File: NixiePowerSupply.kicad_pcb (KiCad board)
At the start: 2 copper layers, 50.8 x 38.1 mm, 12 parts, among them J1 BARREL_JACK, T1 IRF644, U1 MAX1771

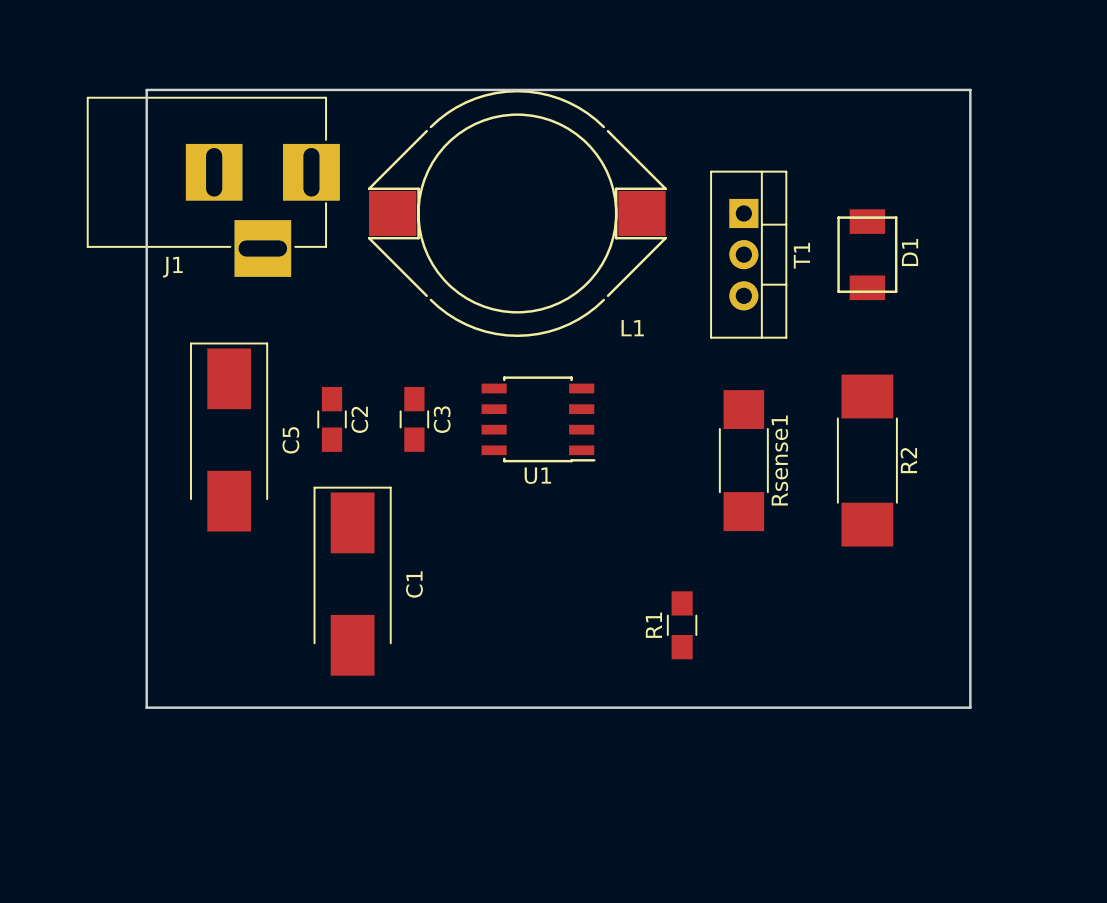
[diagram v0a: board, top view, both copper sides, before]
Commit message: Added cap and trimpot footprints
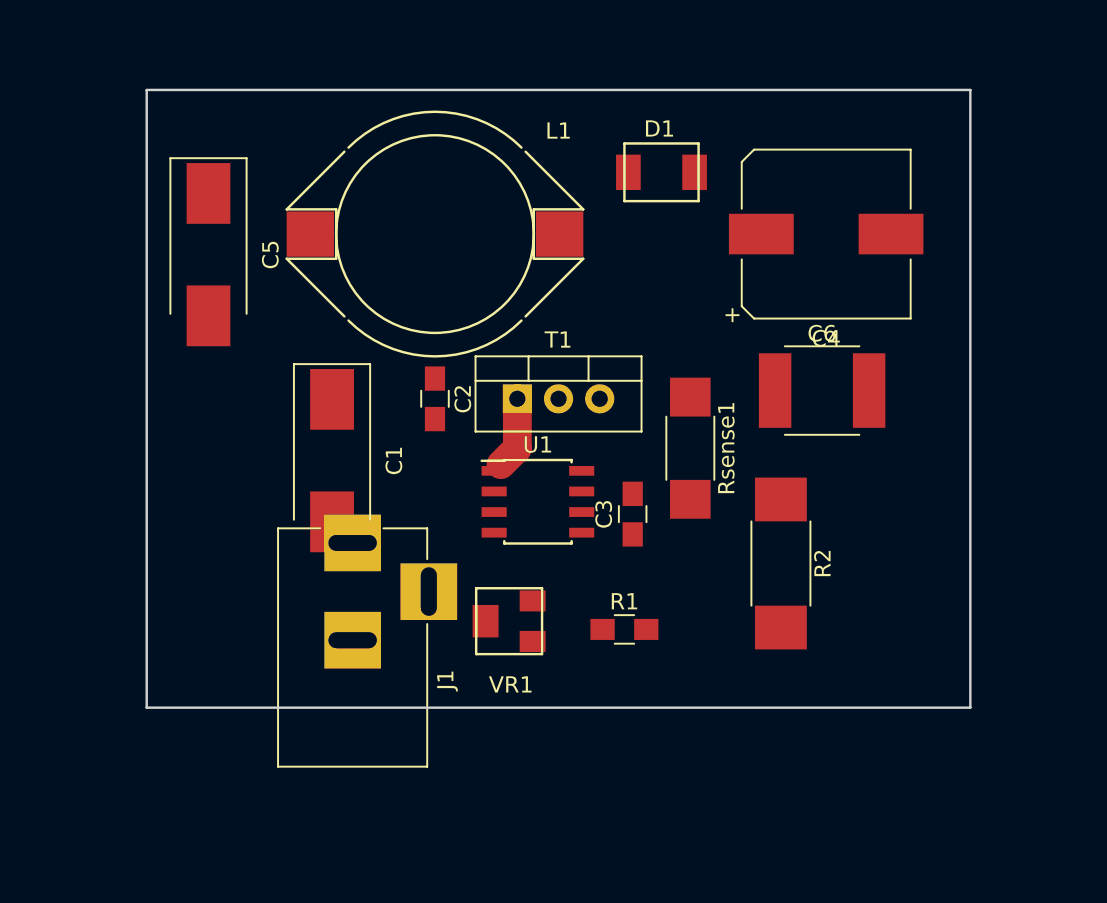
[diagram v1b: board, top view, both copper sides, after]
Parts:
- added C4: 10uF,250V, Capacitors_SMD:CP_Elec_10x10, F.Cu at (166.4, 83.8)
- added C6: 100nF, 250V, nixie:Panasonic_ECWU_Size_B, F.Cu at (166.1, 93.5)
- added VR1: 5K, nixie:Trimpot_Bourns_3214W, F.Cu at (146.8, 107.7)
- moved J1 23.0 mm to (137.2, 102.9), turned to 90 degrees
- moved T1 18.1 mm to (147.3, 94.0), turned to 0 degrees
- moved C3 14.7 mm to (154.4, 101.1), turned to 90 degrees
- moved D1 13.7 mm to (156.2, 80.0), turned to 180 degrees
- moved C5 11.5 mm to (128.3, 85.1)
- moved R2 8.29 mm to (163.6, 104.1)
- moved C1 7.73 mm to (135.9, 97.8)
- moved C2 6.48 mm to (142.2, 94.0)
- moved L1 5.24 mm to (142.2, 83.8)
- moved U1 5.08 mm to (148.6, 100.3), turned to 0 degrees
- moved R1 3.57 mm to (153.9, 108.2), turned to 0 degrees
- moved Rsense1 3.39 mm to (158.0, 97.0)
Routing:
- net Net-(T1-Pad1): track 0.00 -> 4.48 mm
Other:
- net class Gate drive added: clearance 0.254, trace_width 1.778, via_dia 0.6, via_drill 0.4

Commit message: Add headers
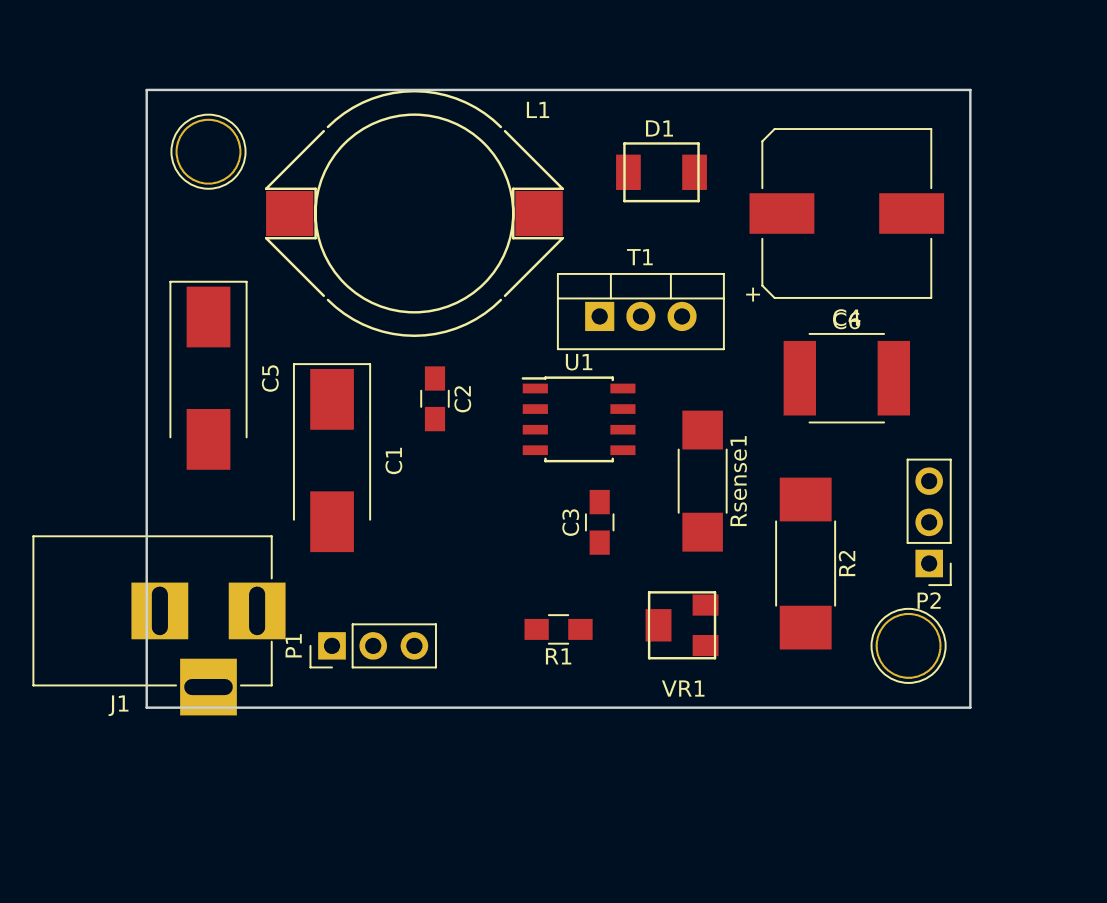
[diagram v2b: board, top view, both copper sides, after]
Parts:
- added P1: CONN_01X03, Pin_Headers:Pin_Header_Straight_1x03_Pitch2.54mm, F.Cu at (135.9, 109.2)
- added P2: CONN_01X03, Pin_Headers:Pin_Header_Straight_1x03_Pitch2.54mm, F.Cu at (172.7, 104.1)
- added REF**: 1pin, Connect:1pin, F.Cu at (128.3, 78.7)
- added REF**: 1pin, Connect:1pin, F.Cu at (171.4, 109.2)
- moved VR1 10.7 mm to (157.5, 108.0)
- moved C5 7.62 mm to (128.3, 92.7)
- moved J1 7.23 mm to (131.3, 107.1), turned to 0 degrees
- moved T1 7.18 mm to (152.4, 88.9)
- moved U1 5.68 mm to (151.1, 95.2)
- moved R1 4.06 mm to (149.9, 108.2), turned to 180 degrees
- moved Rsense1 2.17 mm to (158.8, 99.1)
- moved C3 2.09 mm to (152.4, 101.6)
- moved L1 1.80 mm to (141.0, 82.5)
- moved C4 1.80 mm to (167.6, 82.5)
- moved C6 1.70 mm to (167.6, 92.7)
- moved R2 1.52 mm to (165.1, 104.1)
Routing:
- net Net-(T1-Pad1): track 4.48 -> 0.00 mm

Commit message: More layout; add trimpot model
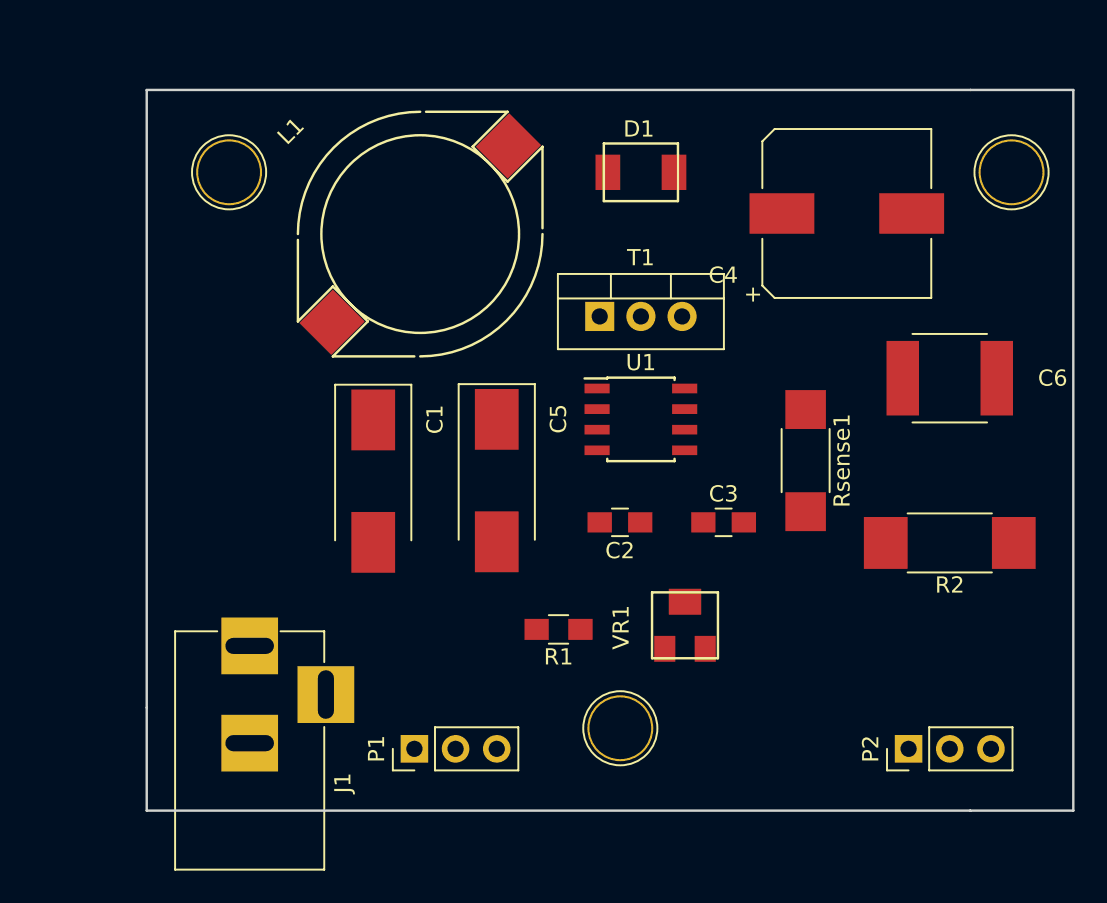
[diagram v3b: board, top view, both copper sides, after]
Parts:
- added REF**: 1pin, Connect:1pin, F.Cu at (153.7, 114.3)
- moved REF** 29.9 mm to (177.8, 80.0)
- moved C5 18.9 mm to (146.1, 99.0)
- moved C2 13.7 mm to (153.7, 101.6), turned to 180 degrees
- moved P2 11.5 mm to (171.4, 115.6), turned to 90 degrees
- moved R2 8.98 mm to (174.0, 102.9), turned to 180 degrees
- moved P1 8.13 mm to (141.0, 115.6)
- moved C3 7.64 mm to (160.0, 101.6), turned to 0 degrees
- moved Rsense1 6.48 mm to (165.1, 97.8)
- moved C6 6.35 mm to (174.0, 92.7)
- moved U1 3.81 mm to (154.9, 95.2)
- moved C1 2.84 mm to (138.4, 99.1)
- moved J1 2.21 mm to (130.8, 109.2), turned to 90 degrees
- moved REF** 1.80 mm to (129.5, 80.0)
- moved L1 1.32 mm to (141.3, 83.8), turned to 45 degrees
- moved D1 1.27 mm to (154.9, 80.0)
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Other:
- board size 50.8 x 38.1 mm -> 57.2 x 44.4 mm
- net class High current added: clearance 0.2, trace_width 0.75, via_dia 0.6, via_drill 0.4

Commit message: Added some tracks.
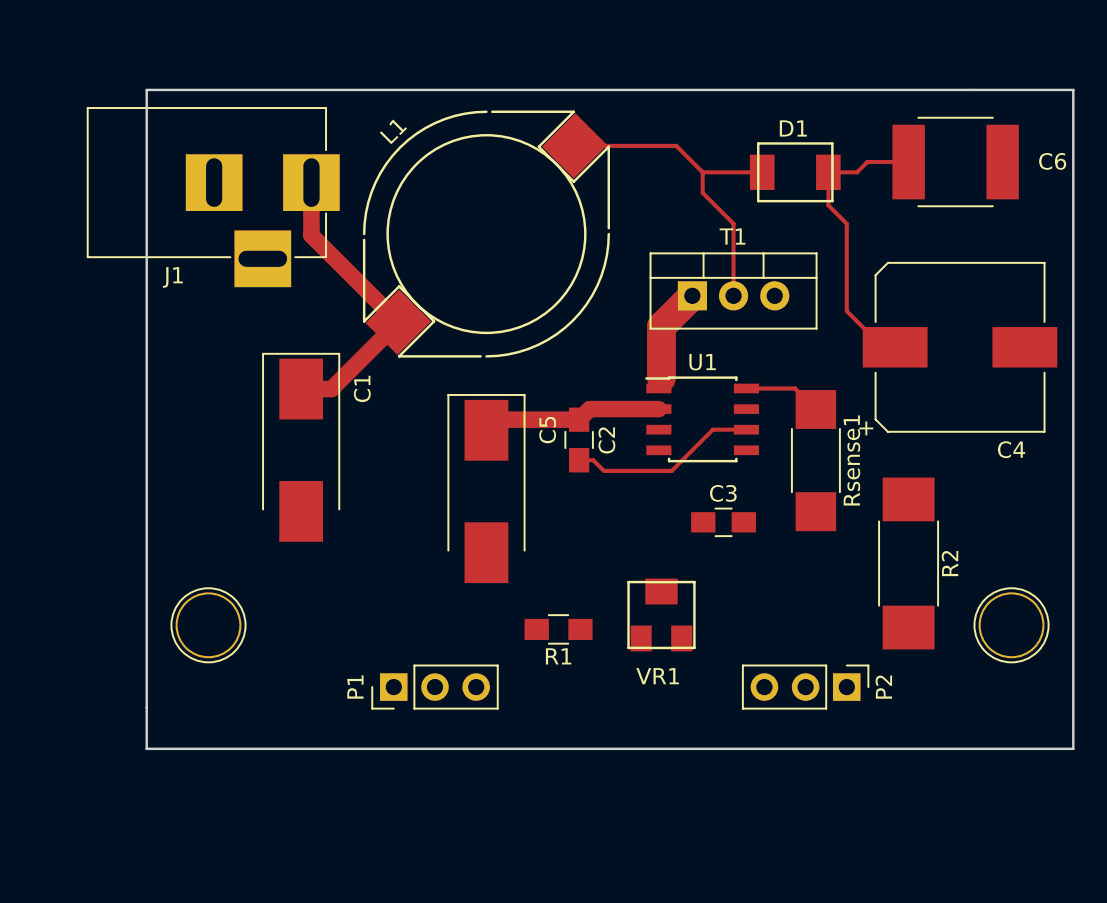
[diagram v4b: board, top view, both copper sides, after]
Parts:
- removed the REF** at (153.7, 114.3)
- moved J1 28.8 mm to (134.6, 80.6), turned to 0 degrees
- moved REF** 28.0 mm to (128.3, 108.0)
- moved REF** 27.9 mm to (177.8, 108.0)
- moved C6 13.3 mm to (174.3, 79.4)
- moved C4 10.8 mm to (174.6, 90.8)
- moved D1 9.53 mm to (164.5, 80.0)
- moved T1 5.85 mm to (158.1, 87.6)
- moved C2 5.67 mm to (151.1, 96.5), turned to 270 degrees
- moved P2 5.39 mm to (167.6, 111.8), turned to 270 degrees
- moved C1 4.84 mm to (134.0, 97.2)
- moved L1 4.09 mm to (145.4, 83.8)
- moved P1 4.02 mm to (139.7, 111.8)
- moved U1 3.81 mm to (158.8, 95.2)
- moved R2 2.84 mm to (171.4, 104.1), turned to 270 degrees
- moved VR1 1.58 mm to (156.2, 107.3)
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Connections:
- net VCC renamed Net-(C1-Pad1)
- C2 pad 2: Net-(C2-Pad2) -> GND
- C3 pad 2: Net-(C2-Pad2) -> GND
- C4 pad 2: Net-(C2-Pad2) -> GND
- C5 pad 2: Net-(C2-Pad2) -> GND
- C6 pad 2: Net-(C2-Pad2) -> GND
- J1 pad 2: Net-(C2-Pad2) -> GND
- J1 pad 3: Net-(J1-Pad3) -> GND
- P2 pad 3: Net-(C2-Pad2) -> GND
- R1 pad 2: Net-(C2-Pad2) -> GND
- Rsense1 pad 2: Net-(C2-Pad2) -> GND
- U1 pad 6: Net-(C2-Pad2) -> GND
- U1 pad 7: Net-(C2-Pad2) -> GND
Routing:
- net Net-(C1-Pad1): track 0.00 -> 29.7 mm
- net Net-(D1-Pad2): track 0.00 -> 20.7 mm
- net Net-(C4-Pad1): track 0.00 -> 18.1 mm
- net GND: track 0.00 -> 11.6 mm
- net Net-(T1-Pad1): track 0.00 -> 5.87 mm
- net Net-(Rsense1-Pad1): track 0.00 -> 4.84 mm
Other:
- board size 57.2 x 44.4 mm -> 57.2 x 40.6 mm
- net class High current: trace_width 0.75 -> 1.016

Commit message: Finished routing
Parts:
- added REF**: 1pin, Connect:1pin, F.Cu at (159.0, 79.2)
- moved C1 5.74 mm to (139.2, 99.6)
- moved R1 4.68 mm to (153.4, 105.2), turned to 90 degrees
- moved D1 3.26 mm to (165.6, 83.1)
- moved VR1 2.37 mm to (158.5, 106.7), turned to 0 degrees
- moved C3 1.53 mm to (161.5, 101.3), turned to 270 degrees
- moved T1 1.28 mm to (158.0, 88.9)
- moved R2 0.80 mm to (171.2, 103.4)
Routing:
- net GND: track 11.6 -> 49.8 mm, vias 0 -> 7
- net Net-(C4-Pad1): track 18.1 -> 44.9 mm
- net Net-(C1-Pad1): track 29.7 -> 56.0 mm
- net Net-(R2-Pad2): track 0.00 -> 23.8 mm
- net Net-(P1-Pad2): track 0.00 -> 23.3 mm
- net Net-(R1-Pad1): track 0.00 -> 7.16 mm
- net Net-(Rsense1-Pad1): track 4.84 -> 11.7 mm
- net Net-(T1-Pad1): track 5.87 -> 0.00 mm
- net Net-(C3-Pad1): track 0.00 -> 2.98 mm
- added copper zone on B.Cu, net GND
- added copper zone on F.Cu, net Net-(T1-Pad1)
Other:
- net class Gate drive: via_dia 0.6 -> 6
- net class High current: trace_width 1.016 -> 1.524

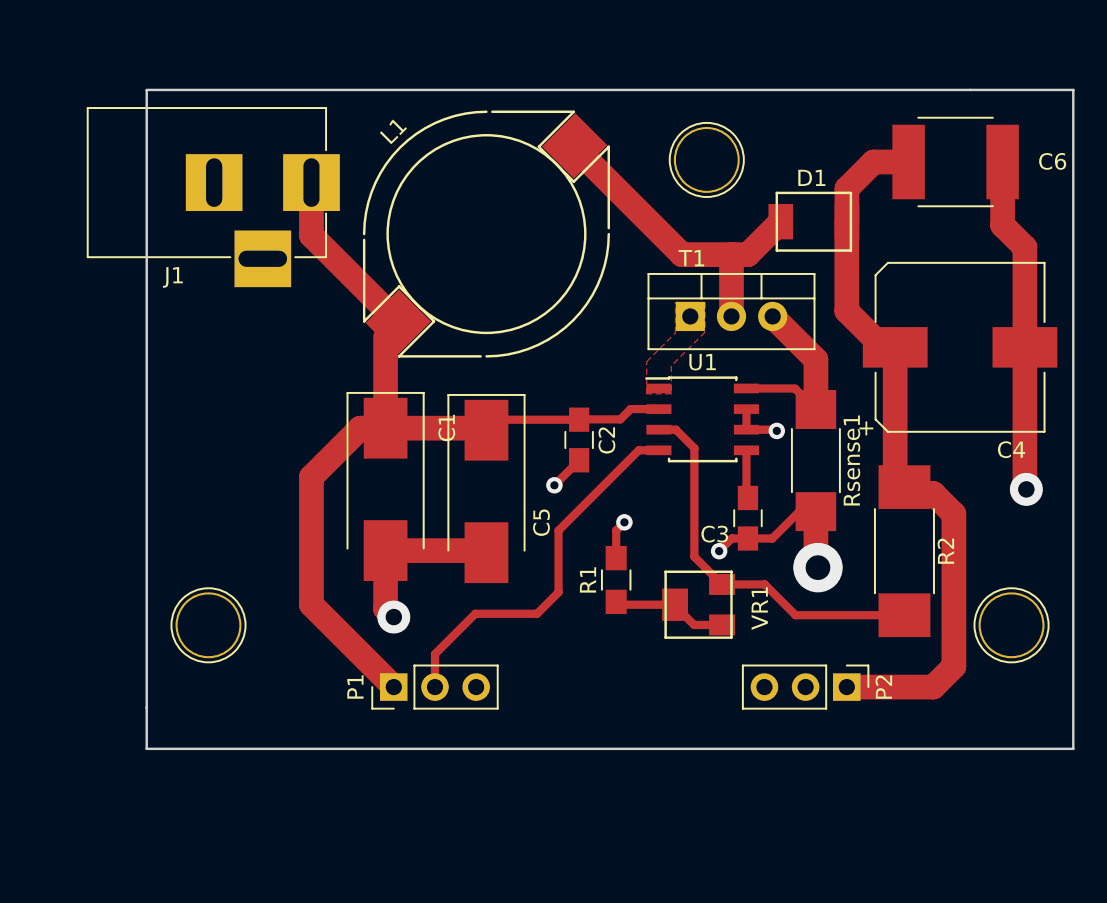
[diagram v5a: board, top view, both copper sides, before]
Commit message: Board re-layout
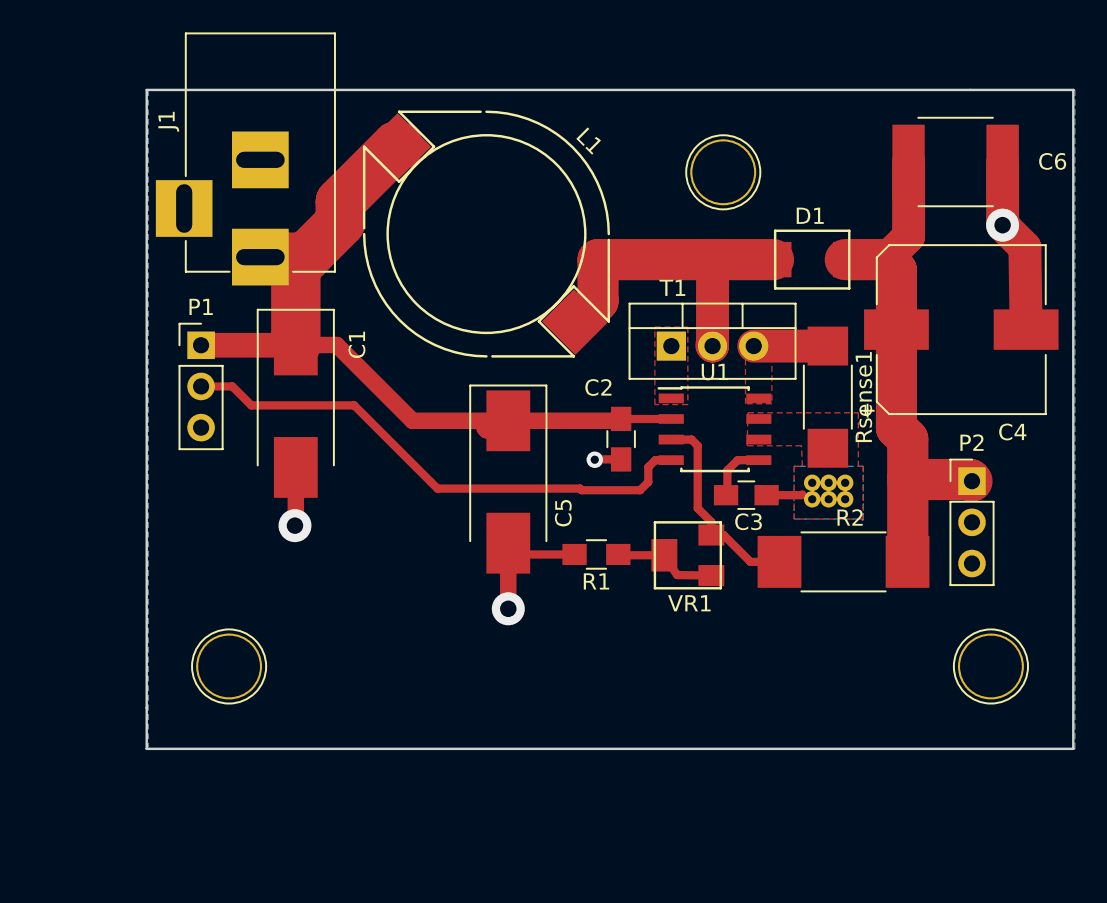
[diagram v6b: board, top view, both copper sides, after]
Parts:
- added REF**: Via, nixie:Via, F.Cu at (167.5, 100.2)
- added REF**: Via, nixie:Via, F.Cu at (166.5, 100.2)
- added REF**: Via, nixie:Via, F.Cu at (165.5, 100.2)
- added REF**: Via, nixie:Via, F.Cu at (167.5, 99.2)
- added REF**: Via, nixie:Via, F.Cu at (166.5, 99.2)
- added REF**: Via, nixie:Via, F.Cu at (165.5, 99.2)
- moved P1 24.2 mm to (127.8, 90.7), turned to 0 degrees
- moved P2 14.9 mm to (175.4, 99.1), turned to 0 degrees
- moved C1 7.55 mm to (133.7, 94.4)
- moved J1 5.57 mm to (131.5, 85.2), turned to 270 degrees
- moved Rsense1 3.98 mm to (166.5, 93.9)
- moved R2 3.82 mm to (167.4, 104.0), turned to 180 degrees
- moved VR1 3.12 mm to (157.8, 103.6)
- moved REF** 2.84 mm to (176.5, 110.5)
- moved REF** 2.84 mm to (129.5, 110.5)
- moved C2 2.59 mm to (153.7, 96.5)
- moved D1 2.34 mm to (165.5, 85.4)
- moved T1 2.17 mm to (156.8, 90.7)
- moved R1 1.99 mm to (152.2, 103.6), turned to 180 degrees
- moved C5 1.47 mm to (146.8, 99.1)
- moved C3 1.43 mm to (161.4, 99.9), turned to 0 degrees
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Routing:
- net GND: track 49.8 -> 27.1 mm, vias 7 -> 4
- net Net-(C4-Pad1): track 44.9 -> 33.1 mm
- net Net-(R2-Pad2): track 23.8 -> 12.5 mm
- net Net-(P1-Pad2): track 23.3 -> 33.5 mm
- net Net-(Rsense1-Pad1): track 11.7 -> 4.57 mm
- net Net-(C1-Pad1): track 56.0 -> 49.9 mm
- net Net-(D1-Pad2): track 20.7 -> 21.5 mm
- net Net-(C3-Pad1): track 2.98 -> 3.76 mm
- net Net-(R1-Pad1): track 7.16 -> 6.44 mm
- added copper zone on F.Cu, net GND
- added copper zone on F.Cu, net Net-(Rsense1-Pad1)
